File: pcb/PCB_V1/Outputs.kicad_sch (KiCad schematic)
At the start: 21 parts, among them J501 FAN1 / 3.5 mm, J511 FAN2 / 3.5 mm, J521 PUMP 24V / 6W, Q501 AO3400A, Q511 AO3400A, Q521 AO3422

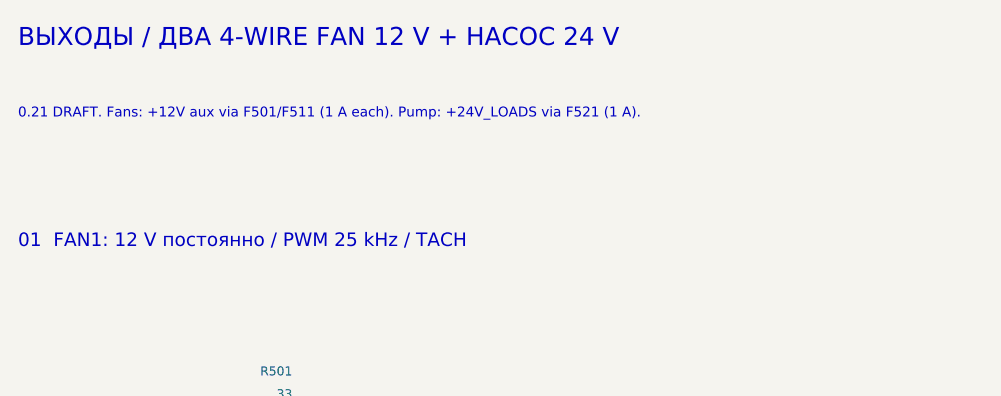
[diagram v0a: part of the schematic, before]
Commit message: pcb: revision 0.22 routing preparation
- Stack confirmed by the user: 1.6 mm, 1 oz outer, 0.5 oz inner.
- LED output MLCCs: Murata GRM32EC72A106KE05L (X7S, 50k in stock) instead
  of TDK; DC-bias digitised from Murata data (2.60 uF at 49 V, model
  2.55 uF), CH1 bank 6.44 uF effective.
- microSD: HRO TF-01A (push-push, C91145) on a project footprint from the
  HRO drawing, checked against the LCSC land; SD passives re-placed.
- TP301 on the PCF8563 CLKOUT for crystal trimming.
- Kelvin net ties NT711/NT712/NT721/NT722 at the LED-driver shunts
  (LED*_CS_K, LED*_FB_K); net ties are excluded from the BOM export.
- analyze_copper.py: IPC-2221 copper screen for the confirmed stack
  (main 24 V path needs pours on both outer layers, via counts).
- L711 and XT60PW-M re-checked and kept; reports v22 and ROUTING_PREP.md.
  USD 30.04 per board (28.42 for five), ERC 0, DRC 0.

Co-Authored-By: Claude Opus 5.5 <noreply@anthropic.com>
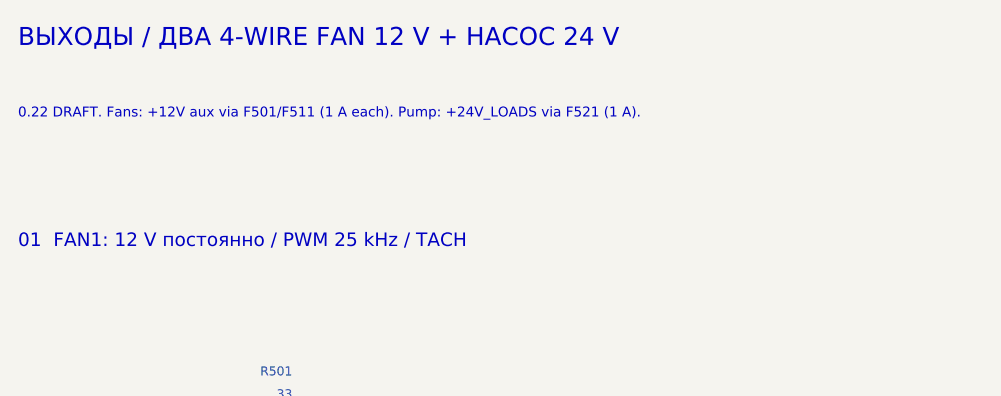
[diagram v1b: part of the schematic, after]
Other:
- note added: "0.22 DRAFT. Fans: +12V aux via F501/F511 (1 A each). Pump: +24V_LOADS via F521 (1 A)."
- note removed: "0.21 DRAFT. Fans: +12V aux via F501/F511 (1 A each). Pump: +24V_LOADS via F521 (1 A)."
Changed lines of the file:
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@@
 		(title "04 - Fans (12 V aux) and pump (24 V)")
 		(date "2026-09-30")
-		(rev "0.21-DRAFT")
+		(rev "0.22-DRAFT")
 		(company "GrowBox controller")
 		(comment 1 "Simplified prototype; unrouted; hardware qualification pending")
@@
 		)
 	)
-	(text "0.21 DRAFT. Fans: +12V aux via F501/F511 (1 A each). Pump: +24V_LOADS via F521 (1 A)."
+	(text "0.22 DRAFT. Fans: +12V aux via F501/F511 (1 A each). Pump: +24V_LOADS via F521 (1 A)."
 		(exclude_from_sim no)
 		(at 20.32 24.13 0)
